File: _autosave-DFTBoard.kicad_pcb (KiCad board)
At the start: 8 copper layers, 141.5 x 58 mm, 304 parts, among them CON1 AVR-JTAG-10, J1 PJ-102A, J10 JACK_TRS_4PINS, J2 AUDIO JACK, J3 AUDIO JACK, J4 AUDIO JACK, J5 JACK_TRS_4PINS, J6 USB_A, J7 USB_B, J8 Micro_SD_Card_Det, J9 HDMI_A, Q1 IRLML2502, Q10 IRLML2502, Q2 IRLML2502, Q3 IRLML2502, Q4 IRLML2502, Q5 IRLML2502, Q6 IRLML2502, Q7 IRLML2502, Q8 IRLML2502, Q9 IRLML2502, SW1 TL6215RF200BDT, U1 LM3880, U10 USB3320, U11 MIC2025-1YMM, U12 USB3320, U13 VL53L0X, U14 APDS-9960, U15 MT41K256M16HA-125_E, U16 MT41K256M16HA-125_E, U17 FTDITypeUART, U18 ABRACON-ASDMB, U19 S25FL256SAGNFI001, U2 LM3880, U20 xc7z020clg484, U21 6N137S, U22 TSOP344, U3 SC189 - 1.0V, U4 SC189 - 3.3V, U5 TLV62080DSGx, U6 LM1085-5.0, U7 SC189 - 1.8V, U8 TPS51200DRCR, U9 TLV320AIC3104, Y1 ABM3-24.000MHZ-D2Y-T, Y2 ABM3-24.000MHZ-D2Y-T

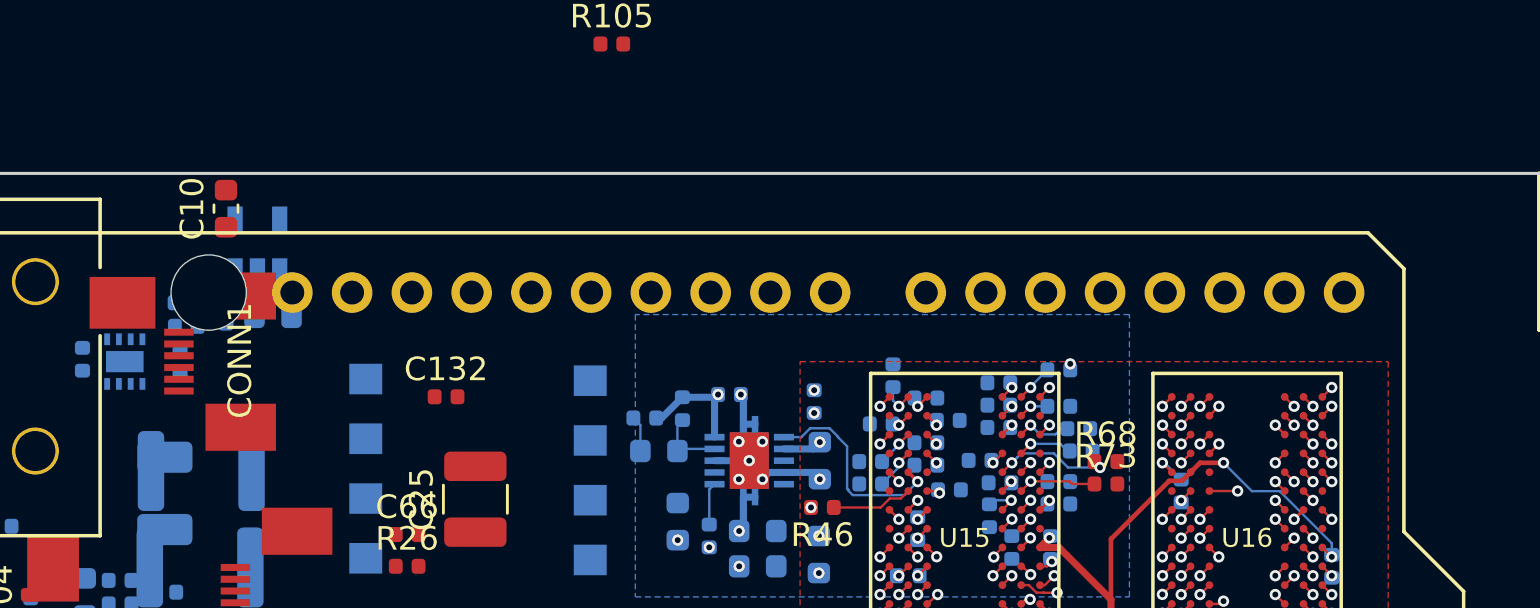
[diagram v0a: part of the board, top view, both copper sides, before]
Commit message: about to remove ZIF screen connector in favor of UNO + RPI
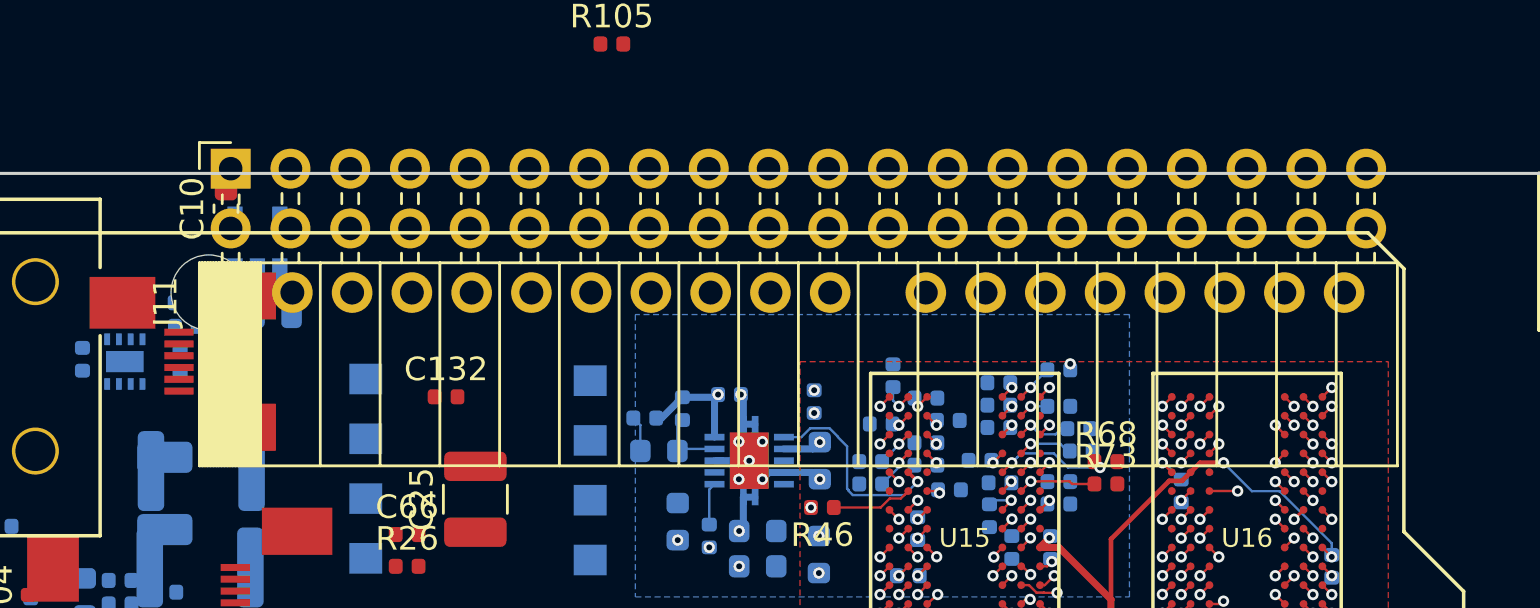
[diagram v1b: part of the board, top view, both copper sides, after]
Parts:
- added J11: Raspberry_Pi_2_3, Connector_PinSocket_2.54mm:PinSocket_2x20_P2.54mm_Horizontal, F.Cu at (157.8, 94.8)
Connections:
- XA1 pad 5V1: (no net) -> +5V
